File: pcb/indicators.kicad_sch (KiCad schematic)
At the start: 8 parts

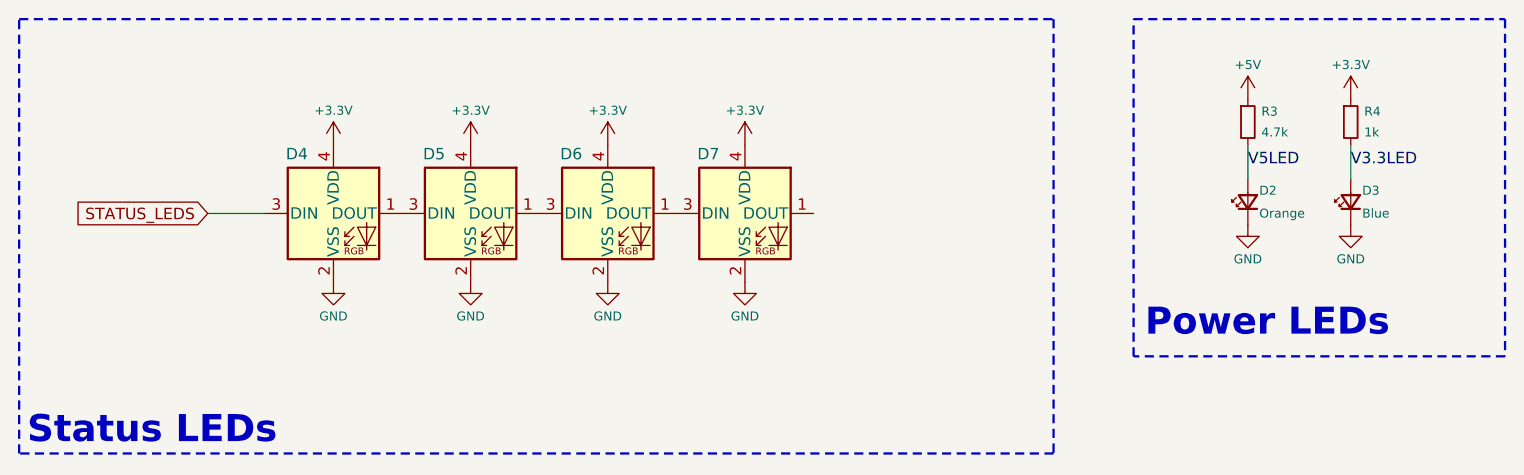
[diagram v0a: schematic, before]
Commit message: Standardized parts; fixed title box
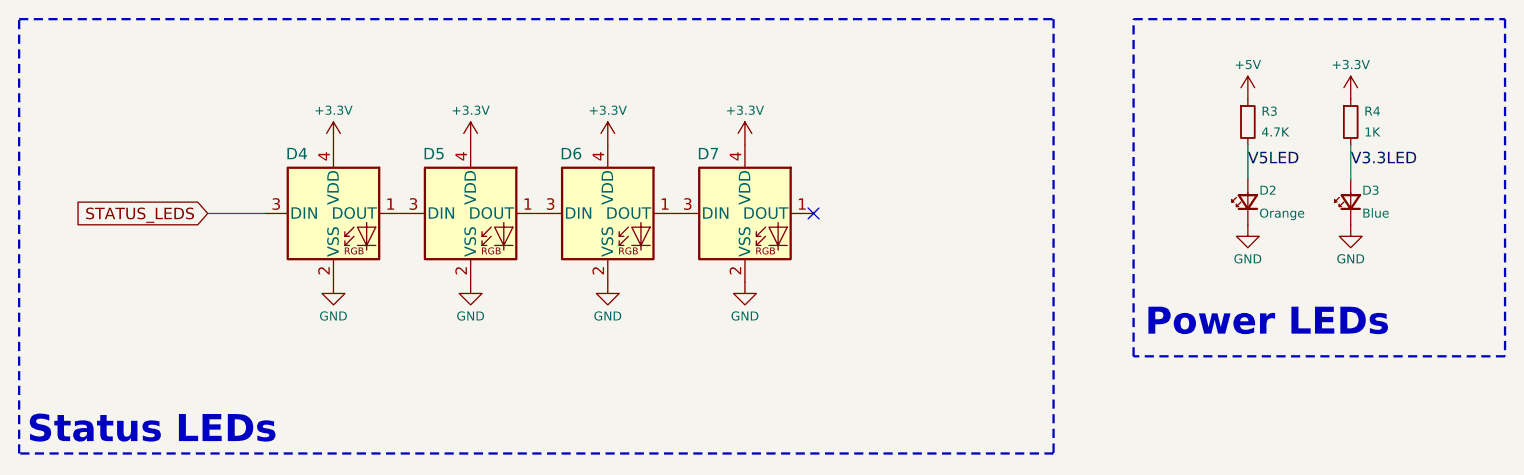
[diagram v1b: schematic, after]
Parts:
- R3: value 4.7k -> 4.7K
- R4: value 1k -> 1K; Digikey 541-1.00KHTR-ND -> 541-3991-2-ND; Mouser 71-CRCW0603-1.0K-E3 -> 71-CRCW06031K00JNEAC
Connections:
- no-connect marks 0 -> 1
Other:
- title: Relay Module -> Servo Module
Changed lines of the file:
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@@
 	(paper "A4")
 	(title_block
-		(title "Relay Module")
+		(title "Servo Module")
 		(date "<<release-date>>")
 		(rev "<<tag>>")
@@
 		)
 	)
+	(no_connect
+		(at 113.03 40.64)
+	)
 	(wire
 		(pts
@@
 			)
 		)
-		(property "Value" "1k"
+		(property "Value" "1K"
 			(at 174.2186 31.623 0)
 			(effects
@@
 			)
 		)
-		(property "Datasheet" "https://www.vishay.com/docs/20035/dcrcwe3.pdf"
+		(property "Datasheet" "https://www.vishay.com/docs/28773/crcwce3.pdf"
 			(at 172.72 30.48 0)
 			(effects
@@
 			)
 		)
-		(property "Mouser" "71-CRCW0603-1.0K-E3"
+		(property "Mouser" "71-CRCW06031K00JNEAC"
 			(at 172.72 30.48 0)
 			(effects
@@
 			)
 		)
-		(property "Digikey" "541-1.00KHTR-ND"
+		(property "Digikey" "541-3991-2-ND"
 			(at 172.72 30.48 0)
 			(effects
@@
 			)
 		)
-		(property "Value" "4.7k"
+		(property "Value" "4.7K"
 			(at 162.7886 31.623 0)
 			(effects

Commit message: Reworked based on new standards
Decreased to 3 servo ports
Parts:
- removed D2: Orange, LED_SMD:LED_0603_1608Metric, symbol Device:LED_Small
- removed D3: Blue, LED_SMD:LED_0603_1608Metric, symbol Device:LED_Small
- removed D4, D5, D6, D7: WS2812B-2020, LED_SMD:LED_WS2812B-2020_PLCC4_2.0x2.0mm, symbol LED:WS2812B-2020
- removed R3: 4.7K, Resistor_SMD:R_0603_1608Metric, symbol Device:R_Small
- removed R4: 1K, Resistor_SMD:R_0603_1608Metric, symbol Device:R_Small
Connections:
- no-connect marks 1 -> 0
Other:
- note removed: "Power LEDs"
- note removed: "Status LEDs"
